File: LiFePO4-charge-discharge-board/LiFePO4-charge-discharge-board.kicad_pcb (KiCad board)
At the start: 2 copper layers, 22 x 15.5 mm, 10 parts, among them J1 Conn_JST-XH_1x2, J2 mech.-solder-pad_1x2, U1 LiFePO4-Charge

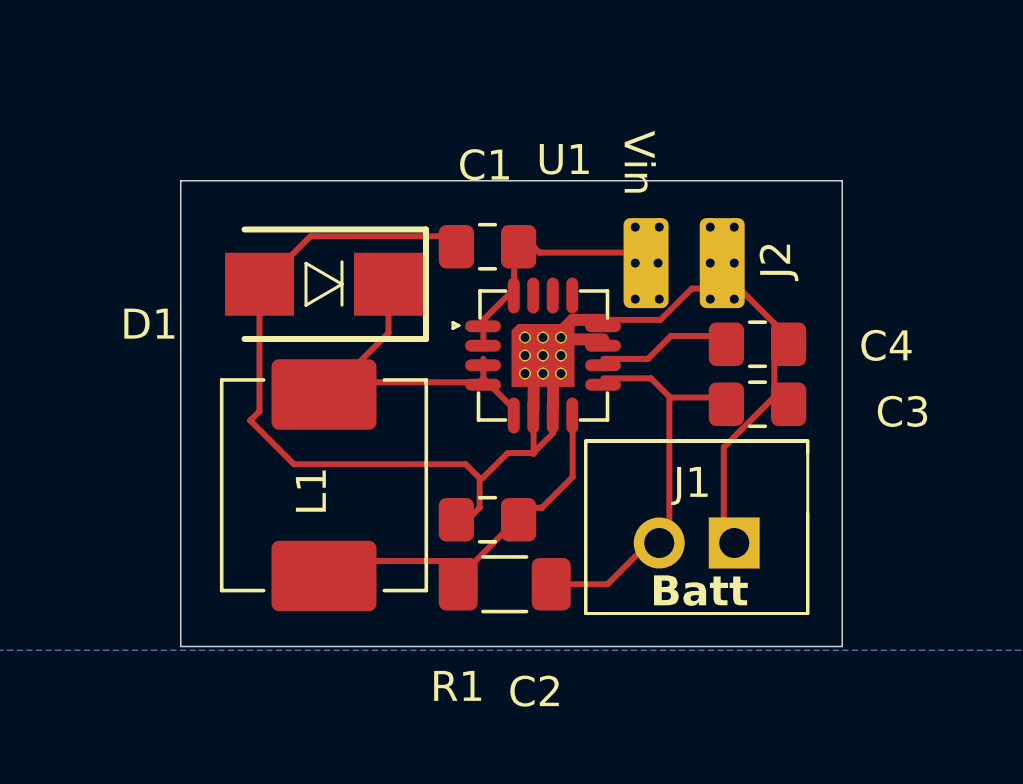
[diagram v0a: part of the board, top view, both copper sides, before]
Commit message: Add Working charge section
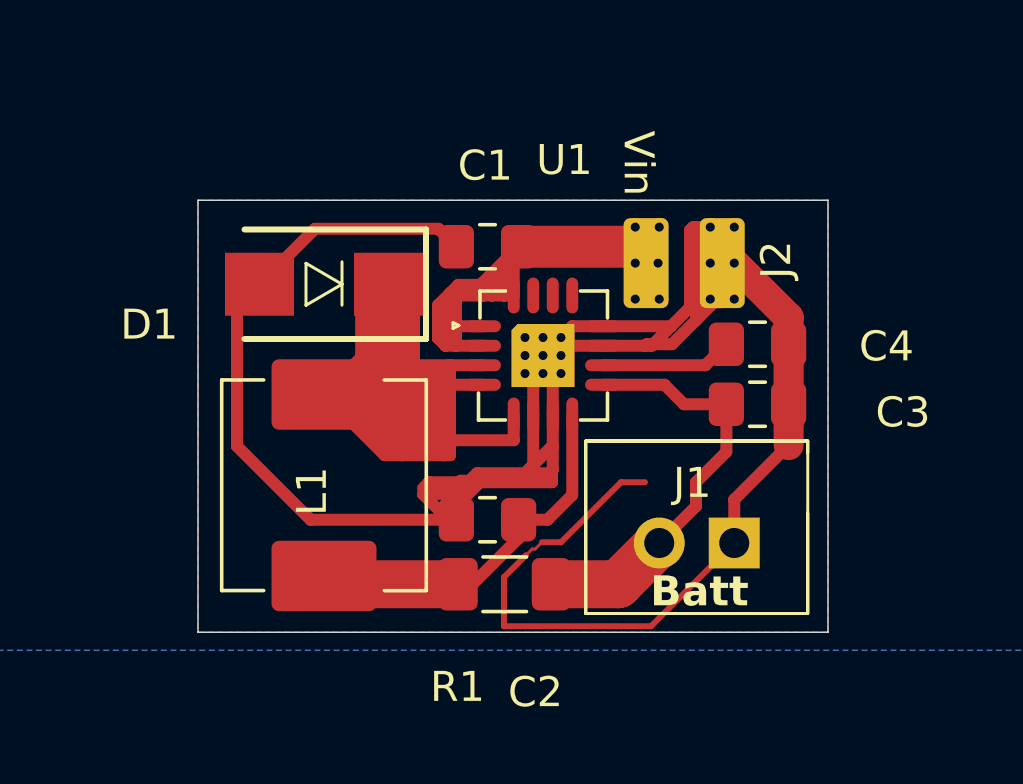
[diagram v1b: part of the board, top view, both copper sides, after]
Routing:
- net Net-(D1-K): track 11.6 -> 58.8 mm
- net GND: track 50.7 -> 91.8 mm
- net Vin: track 8.54 -> 22.2 mm
- net Net-(U1-BAT): track 13.0 -> 13.7 mm
- added copper zone on F.Cu, net GND
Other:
- board size 22 x 15.5 mm -> 21 x 14.4 mm

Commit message: rewire circuit
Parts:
- added C5: 47u, Capacitor_SMD:C_0805_2012Metric_Pad1.18x1.45mm_HandSolder, F.Cu at (142.6, 99.2)
- added C6: 47u, Capacitor_SMD:C_0805_2012Metric_Pad1.18x1.45mm_HandSolder, F.Cu at (142.6, 107.4)
- added IC1: RT6150B-33GQW, Marcus-PCB-Library:SON50P250X250X80-11N-D, F.Cu at (142.6, 103.2)
- added J3: mech.-solder-pad_1x2, Marcus-PCB-Library:Conn_Mechc.-solder-pad_1x2, F.Cu at (128.2, 114.4)
- added L2: 2,2uH, Inductor_SMD:L_APV_APH0630, F.Cu at (135.5, 103.1)
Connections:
- net Net-(U1-BAT) renamed VBatt
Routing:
- net VBatt: track 13.7 -> 45.9 mm
- net Vout: track 0.00 -> 16.8 mm
- net GND: track 91.8 -> 79.7 mm
- net Net-(IC1-LX1): track 0.00 -> 10.5 mm
- net Net-(IC1-LX2): track 0.00 -> 9.78 mm
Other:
- board size 21 x 14.4 mm -> 46 x 21 mm

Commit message: Finish version V1.0
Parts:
- removed J3: mech.-solder-pad_1x2, Marcus-PCB-Library:Conn_Mechc.-solder-pad_1x2
- added C7: 1uF, Capacitor_SMD:C_0603_1608Metric, F.Cu at (37.5, 34.5)
- added IC2: APX810S-31SA-7, Marcus_ICs:SOT-23-3_Marcus, F.Cu at (35.1, 34.9)
- added J7: Conn_Castellation_1x2_no_GND, Marcus_Connectors:Conn_Castellated_1x2_no_GND, F.Cu at (37.0, 25.5)
- added Q1: AO3415, Marcus_ICs:SOT-23-3_Marcus, F.Cu at (35.1, 30.8)
- added R2: R, Resistor_SMD:R_0603_1608Metric, F.Cu at (32.1, 32.8)
- added R3: R, Resistor_SMD:R_0603_1608Metric, F.Cu at (29.1, 32.8)
- added R4: R, Resistor_SMD:R_0603_1608Metric, F.Cu at (32.6, 35.9)
- added R5: R, Resistor_SMD:R_0603_1608Metric, F.Cu at (32.5, 39.3)
- added SW1: Switch, Marcus_Connectors:Conn_Mechc.-solder-pad_1x2, F.Cu at (37.6, 39.0)
- C1, C2, C3, C5, C6: footprint Capacitor_SMD:C_0805_2012Metric_Pad1.18x1.45mm_HandSolder -> Capacitor_SMD:C_0805_2012Metric
- C4: value 100nF -> 1uF; footprint Capacitor_SMD:C_0805_2012Metric_Pad1.18x1.45mm_HandSolder -> Capacitor_SMD:C_0603_1608Metric
- D1: value SS34B-HF -> PMEG10020ELXEX; footprint Marcus-PCB-Library:DIOM5336X320N -> Marcus_Discretes:PMEG4010EXEX
- IC1: footprint Marcus-PCB-Library:SON50P250X250X80-11N-D -> Marcus_ICs:SON50P250X250X80-11N-D
- J1: footprint Marcus-PCB-Library:Conn_JST-XH_1x2 -> Marcus_Connectors:Conn_JST-XH_1x2
- J2: value mech.-solder-pad_1x2 -> Conn_Castellation_1x3; footprint Marcus-PCB-Library:Conn_Mechc.-solder-pad_1x2 -> Marcus_Connectors:Conn_Castellated_1x3_GND_moved
- L1, L2: footprint Inductor_SMD:L_APV_APH0630 -> Marcus_Passives:INDC3225X120N
- R1: footprint Resistor_SMD:R_1206_3216Metric_Pad1.30x1.75mm_HandSolder -> Resistor_SMD:R_1206_3216Metric
- U1: value LiFePO4-Charge -> TP5000-QFN16; footprint Marcus-PCB-Library:TP5000-QFN16 -> Marcus_ICs:TP5000-QFN16
- moved C6 131.7 mm to (29.6, 39.7), turned to 0 degrees
- moved IC1 130.8 mm to (29.7, 37.1)
- moved C5 130.5 mm to (29.3, 34.5), turned to 0 degrees
- moved L2 128.8 mm to (24.2, 38.4)
- moved J2 127.2 mm to (21.5, 23.0)
- moved J1 123.7 mm to (25.0, 33.5)
- moved C3 121.8 mm to (31.4, 24.7)
- moved C4 121.5 mm to (31.5, 23.0)
- moved U1 120.5 mm to (25.5, 23.6)
- moved R1 115.8 mm to (30.7, 30.9)
- moved C2 115.2 mm to (32.1, 27.4), turned to 90 degrees
- moved C1 113.6 mm to (31.6, 21.3), turned to 0 degrees
- moved L1 112.1 mm to (29.5, 27.7), turned to 90 degrees
- moved D1 104.9 mm to (34.4, 26.4), turned to 90 degrees
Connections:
- IC1 pad 7: VBatt -> /power_save
- J1 pad 2: VBatt -> /VBatt3
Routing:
- net Net-(D1-Pad1): track 58.8 -> 14.7 mm
- net /VBatt3: track 0.00 -> 19.2 mm
- net /power_save: track 0.00 -> 17.1 mm, vias 0 -> 1
- net /Batt_monitor: track 0.00 -> 16.1 mm, vias 0 -> 1
- net /VBatt2: track 0.00 -> 13.1 mm
- net GND: track 79.7 -> 73.2 mm, vias 0 -> 34
- net VBatt: track 45.9 -> 40.0 mm, vias 0 -> 7
- net Net-(IC1-LX2): track 9.78 -> 4.46 mm
- net Net-(IC1-LX1): track 10.5 -> 5.24 mm
- net Net-(IC2-RESET): track 0.00 -> 3.29 mm
- net Vout: track 16.8 -> 15.7 mm, vias 0 -> 2
- net Vin: track 22.2 -> 22.0 mm, vias 0 -> 4
- net Net-(U1-VS): track 12.2 -> 12.3 mm, vias 0 -> 2
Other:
- board size 46 x 21 mm -> 18.5 x 21 mm
- board text added: "2"
- board text added: "3.3V"
- board text added: "4"
- board text added: "5"
- board text added: "B+ B-"
- board text added: "B- B+"
- board text added: "Bmon"
- board text added: "G"
- board text added: "L1"
- board text added: "L2"
- board text added: "LiFePO4 charge-discharge Module V1.0"
- board text added: "PS"
- board text added: "Vin"
- board text added: "Vout"
